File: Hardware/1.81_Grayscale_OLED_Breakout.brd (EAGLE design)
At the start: 15.2 x 35.6 mm, 31 parts, among them U1 1.25V 500mA, U2 3.3V, U3 TXB0104

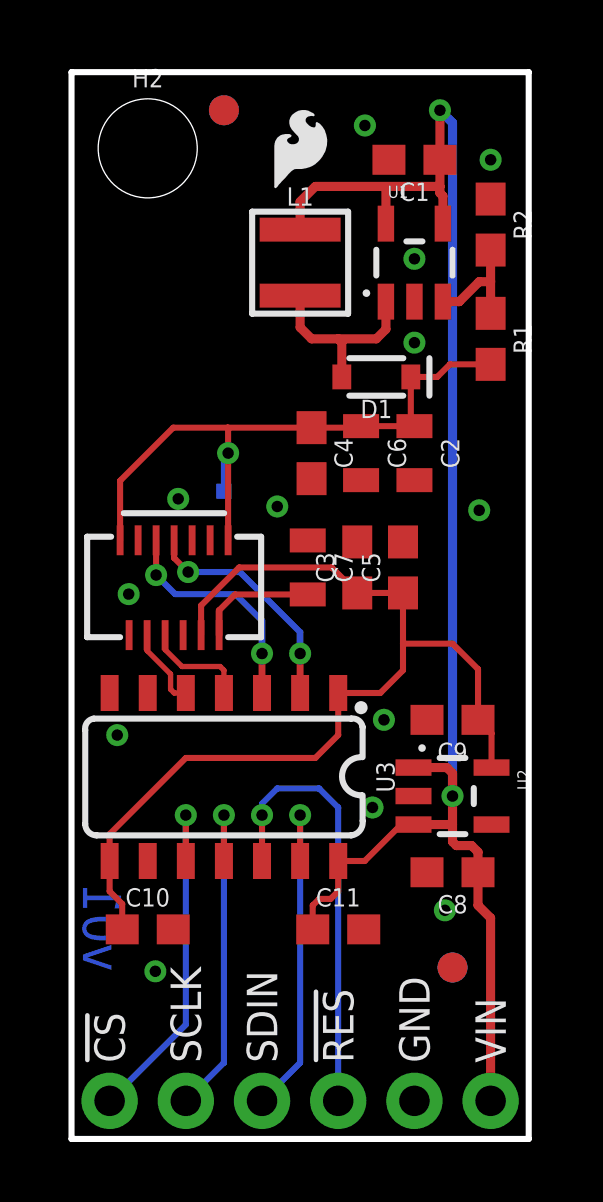
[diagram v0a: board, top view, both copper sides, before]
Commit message: added panel
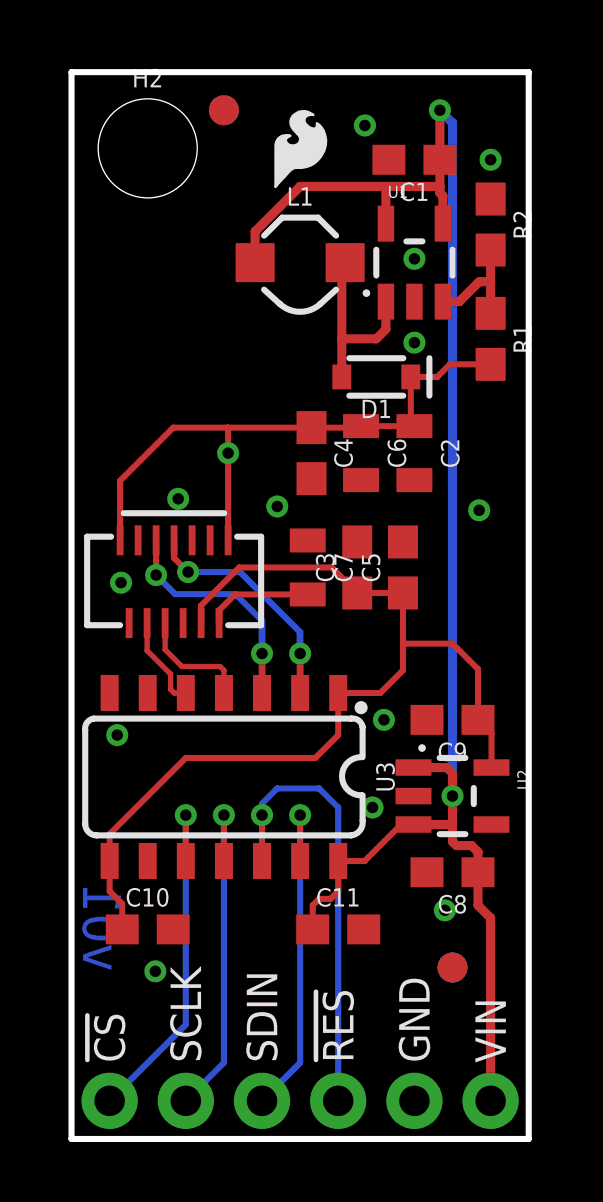
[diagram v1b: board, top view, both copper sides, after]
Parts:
- removed TP1: TEST-POINT2, SparkFun-Connectors:PAD.02X.02
- L1: device SparkFun-Coils:INDUCTOR_3X3 -> SparkFun-Coils:INDUCTOR_4.7UH
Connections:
- net 12V: no longer TP1.P$1
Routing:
- net VIN: track 54.2 -> 56.2 mm
- net 12V: track 22.2 -> 21.0 mm
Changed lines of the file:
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@@
 <attribute name="PROD_ID" value="DIO-11623" x="10.16" y="25.4" size="1.778" layer="27" font="vector" ratio="15" rot="R180" display="off"/>
 </element>
-<element name="L1" library="SparkFun-Coils" package="INDUCTOR_3X3" value="10uH" x="7.62" y="29.21" smashed="yes">
+<element name="L1" library="SparkFun-Coils" package="INDUCTOR_4.7UH" value="10uH" x="7.62" y="29.21" smashed="yes">
 <attribute name="NAME" x="7.62" y="31.11" size="0.6096" layer="25" ratio="20" align="bottom-center"/>
 <attribute name="VALUE" x="7.62" y="31.75" size="0.6096" layer="27" ratio="20" align="top-center"/>
-<attribute name="PROD_ID" value="NDUC-13913" x="7.62" y="29.21" size="1.778" layer="27" display="off"/>
+<attribute name="PROD_ID" value="NDUC-09819" x="7.62" y="29.21" size="1.778" layer="27" display="off"/>
 </element>
 <element name="C3" library="SparkFun-Capacitors" package="0603" value="0.1uF" x="9.525" y="19.05" smashed="yes" rot="R90">
@@
 <element name="FD2" library="SparkFun-Aesthetics" package="FIDUCIAL-1X2" value="FIDUCIAL1X2" x="5.08" y="34.29"/>
 <element name="DS1" library="SparkFun-Displays" package="OEL_1.8_FPC_Y3B" value="OEL_1.8OEL_Y3B" x="7.62" y="31.75" rot="MR0">
-<attribute name="PROD_ID" value="LCD-13910" x="7.62" y="31.75" size="1.778" layer="28" rot="MR0" display="off"/>
+<attribute name="PROD_ID" value="LCD-13910, CONN-13933" x="7.62" y="31.75" size="1.778" layer="28" rot="MR0" display="off"/>
 </element>
 <element name="LOGO2" library="SparkFun-Aesthetics" package="REVISION" value="REVISION" x="-11.43" y="-11.43"/>
@@
 <element name="LOGO3" library="SparkFun-Aesthetics" package="SFE_LOGO_FLAME_.1" value="SFE_LOGO_FLAME.1_INCH" x="6.477" y="31.369"/>
 <element name="LOGO4" library="SparkFun-Aesthetics" package="OSHW-LOGO-S" value="OSHW-LOGOS" x="7.62" y="33.02" rot="MR0"/>
-<element name="TP1" library="SparkFun-Connectors" package="PAD.02X.02" value="TEST-POINT2" x="5.08" y="21.59" rot="MR0"/>
 </elements>
 <signals>
@@
 <via x="10.033" y="11.049" extent="1-16" drill="0.381"/>
 <via x="12.446" y="7.62" extent="1-16" drill="0.381"/>
-<via x="1.905" y="18.161" extent="1-16" drill="0.381"/>
+<via x="1.651" y="18.542" extent="1-16" drill="0.381"/>
 <via x="13.589" y="20.955" extent="1-16" drill="0.381"/>
 <via x="11.43" y="26.543" extent="1-16" drill="0.381"/>
@@
 <wire x1="12.28" y1="31.75" x2="12.28" y2="31.53" width="0.3048" layer="1"/>
 <wire x1="12.28" y1="31.53" x2="12.38" y2="31.43" width="0.3048" layer="1"/>
-<wire x1="7.62" y1="30.31" x2="7.62" y2="31.242" width="0.3048" layer="1"/>
-<wire x1="7.62" y1="31.242" x2="8.128" y2="31.75" width="0.3048" layer="1"/>
-<wire x1="8.128" y1="31.75" x2="10.16" y2="31.75" width="0.3048" layer="1"/>
+<wire x1="7.62" y1="31.75" x2="10.48" y2="31.75" width="0.3048" layer="1"/>
 <wire x1="10.48" y1="31.75" x2="12.28" y2="31.75" width="0.3048" layer="1"/>
 <wire x1="10.48" y1="30.5101" x2="10.48" y2="31.75" width="0.3048" layer="1"/>
-<wire x1="10.48" y1="31.75" x2="10.16" y2="31.75" width="0.3048" layer="1"/>
+<wire x1="7.62" y1="31.75" x2="6.12" y2="30.25" width="0.3048" layer="1"/>
+<wire x1="6.12" y1="30.25" x2="6.12" y2="29.21" width="0.3048" layer="1"/>
 </signal>
 <signal name="N$2">
@@
 <wire x1="10.48" y1="27.9099" x2="10.48" y2="26.99" width="0.3048" layer="1"/>
 <wire x1="10.48" y1="26.99" x2="10.16" y2="26.67" width="0.3048" layer="1"/>
-<wire x1="10.16" y1="26.67" x2="8.89" y2="26.67" width="0.3048" layer="1"/>
-<wire x1="8.89" y1="26.67" x2="8.001" y2="26.67" width="0.3048" layer="1"/>
-<wire x1="9.01" y1="25.4" x2="9.01" y2="26.55" width="0.3048" layer="1"/>
-<wire x1="9.01" y1="26.55" x2="8.89" y2="26.67" width="0.3048" layer="1"/>
-<wire x1="7.62" y1="28.11" x2="7.62" y2="27.051" width="0.3048" layer="1"/>
-<wire x1="7.62" y1="27.051" x2="8.001" y2="26.67" width="0.3048" layer="1"/>
+<wire x1="9.01" y1="25.4" x2="9.01" y2="26.67" width="0.3048" layer="1"/>
+<wire x1="9.01" y1="26.67" x2="9.01" y2="29.1" width="0.3048" layer="1"/>
+<wire x1="9.01" y1="29.1" x2="9.12" y2="29.21" width="0.254" layer="1"/>
+<wire x1="10.16" y1="26.67" x2="9.01" y2="26.67" width="0.3048" layer="1"/>
 </signal>
 <signal name="N$3">
@@
 <wire x1="13.97" y1="25.82" x2="12.612" y2="25.82" width="0.2032" layer="1"/>
 <wire x1="12.612" y1="25.82" x2="12.192" y2="25.4" width="0.2032" layer="1"/>
-<contactref element="TP1" pad="P$1"/>
-<wire x1="5.08" y1="21.59" x2="5.08" y2="22.72" width="0.2032" layer="16"/>
 <wire x1="5.08" y1="22.72" x2="5.22" y2="22.86" width="0.2032" layer="16"/>
 <via x="5.22" y="22.86" extent="1-16" drill="0.381"/>
@@
 <contactref element="C7" pad="2"/>
 <contactref element="DS1" pad="12"/>
-<wire x1="4.92" y1="16.795" x2="4.92" y2="17.62" width="0.2286" layer="1"/>
+<wire x1="4.92" y1="17.195" x2="4.92" y2="17.62" width="0.2286" layer="1"/>
 <wire x1="4.92" y1="17.62" x2="5.45" y2="18.15" width="0.2032" layer="1"/>
 <wire x1="5.45" y1="18.15" x2="7.874" y2="18.15" width="0.2032" layer="1"/>
@@
 <wire x1="3.81" y1="12.7" x2="8.128" y2="12.7" width="0.2032" layer="1"/>
 <contactref element="DS1" pad="10"/>
-<wire x1="4.32" y1="16.795" x2="4.32" y2="17.782" width="0.2032" layer="1"/>
+<wire x1="4.32" y1="17.195" x2="4.32" y2="17.782" width="0.2032" layer="1"/>
 <wire x1="4.32" y1="17.782" x2="5.588" y2="19.05" width="0.2032" layer="1"/>
 <wire x1="5.588" y1="19.05" x2="8.675" y2="19.05" width="0.2032" layer="1"/>
@@
 <wire x1="3.423" y1="14.865" x2="3.302" y2="14.986" width="0.1778" layer="1"/>
 <wire x1="3.302" y1="14.986" x2="3.302" y2="15.494" width="0.1778" layer="1"/>
-<wire x1="2.52" y1="16.795" x2="2.52" y2="16.276" width="0.1778" layer="1"/>
+<wire x1="2.52" y1="17.195" x2="2.52" y2="16.276" width="0.1778" layer="1"/>
 <wire x1="2.52" y1="16.276" x2="3.302" y2="15.494" width="0.1778" layer="1"/>
 </signal>
@@
 <wire x1="5.08" y1="14.865" x2="5.08" y2="15.621" width="0.1778" layer="1"/>
 <wire x1="5.08" y1="15.621" x2="4.953" y2="15.748" width="0.1778" layer="1"/>
-<wire x1="3.12" y1="16.795" x2="3.12" y2="16.311" width="0.1778" layer="1"/>
+<wire x1="3.12" y1="17.195" x2="3.12" y2="16.311" width="0.1778" layer="1"/>
 <wire x1="3.12" y1="16.311" x2="3.683" y2="15.748" width="0.1778" layer="1"/>
 <wire x1="3.683" y1="15.748" x2="4.953" y2="15.748" width="0.1778" layer="1"/>

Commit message: post checklist changes
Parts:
- added TP1, TP2, TP3, TP4, TP5, TP6, TP7: TEST-POINT3, SparkFun-Connectors:PAD.03X.03
- U1: value 1.25V 500mA -> AP3012
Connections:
- net !CS!: now also TP2.P$1
- net !RES!: now also TP1.P$1
- net 12V: now also TP7.P$1
- net 3.3V: now also TP6.P$1
- net N$1: now also TP5.P$1
- net SCLK: now also TP3.P$1
- net SDIN: now also TP4.P$1
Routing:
- net N$1: track 3.60 -> 11.7 mm, vias 0 -> 1
- net !CS!: track 3.09 -> 6.51 mm, vias 0 -> 1
- net SCLK: track 3.89 -> 6.40 mm, vias 0 -> 1
- net SDIN: track 7.84 -> 10.0 mm
- net !RES!: track 7.73 -> 9.66 mm
- net 3.3V: track 33.3 -> 35.0 mm, vias 0 -> 1
- net 12V: track 21.0 -> 22.2 mm, vias 1 -> 2
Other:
- board text added: "v10"
- board text removed: "v01"
